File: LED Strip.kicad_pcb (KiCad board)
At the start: 2 copper layers, 20 x 12 mm, 9 parts, among them J1 CONN_01X02

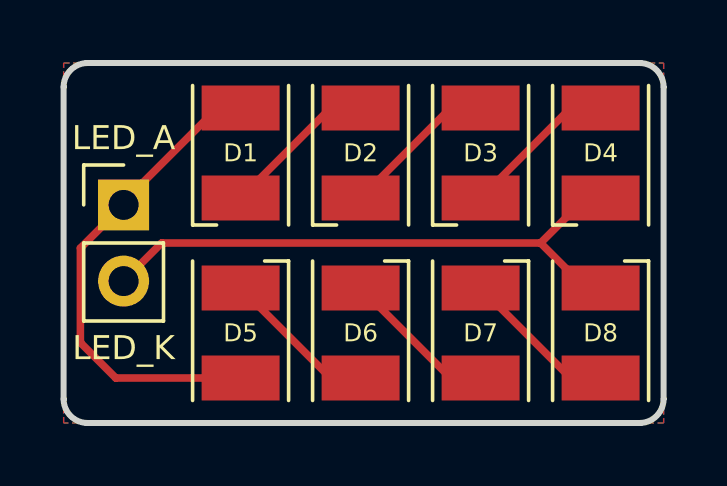
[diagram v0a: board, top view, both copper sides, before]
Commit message: Adds project name and version to silkscreen Adds OSH logo to bottom copper layer Generated gerber files
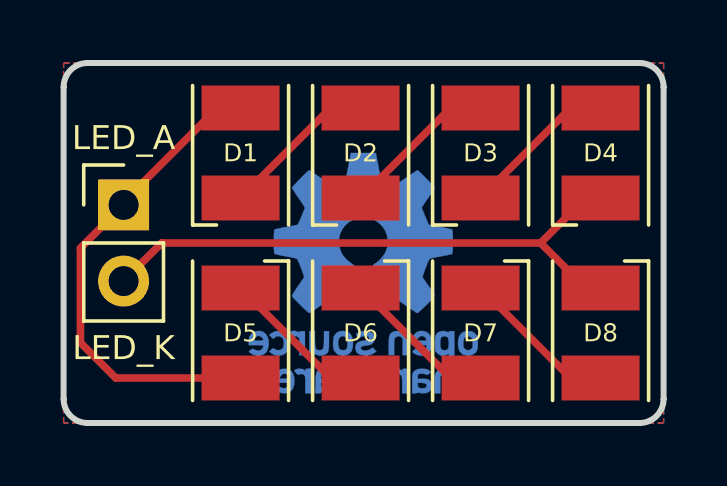
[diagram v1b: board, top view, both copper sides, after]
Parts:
- added OSHW-Logo: OSHW-Logo_7.5x8mm_Copper, Symbols:OSHW-Logo_7.5x8mm_Copper, B.Cu at (110.0, 95.0)
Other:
- board text added: "LED Strip - CLM3C v1.0"
